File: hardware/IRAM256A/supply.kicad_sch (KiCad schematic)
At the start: 65 parts

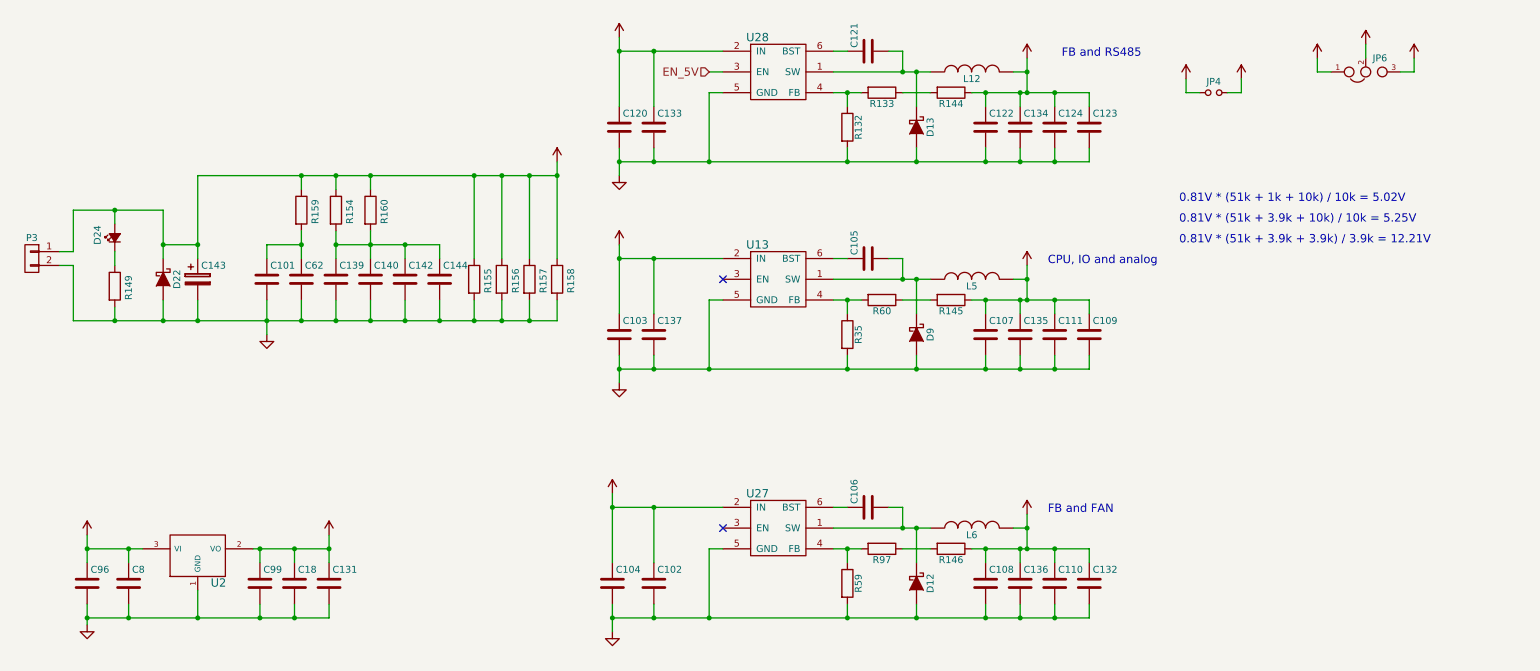
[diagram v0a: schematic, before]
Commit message: Structure change + kicad 3d models updated
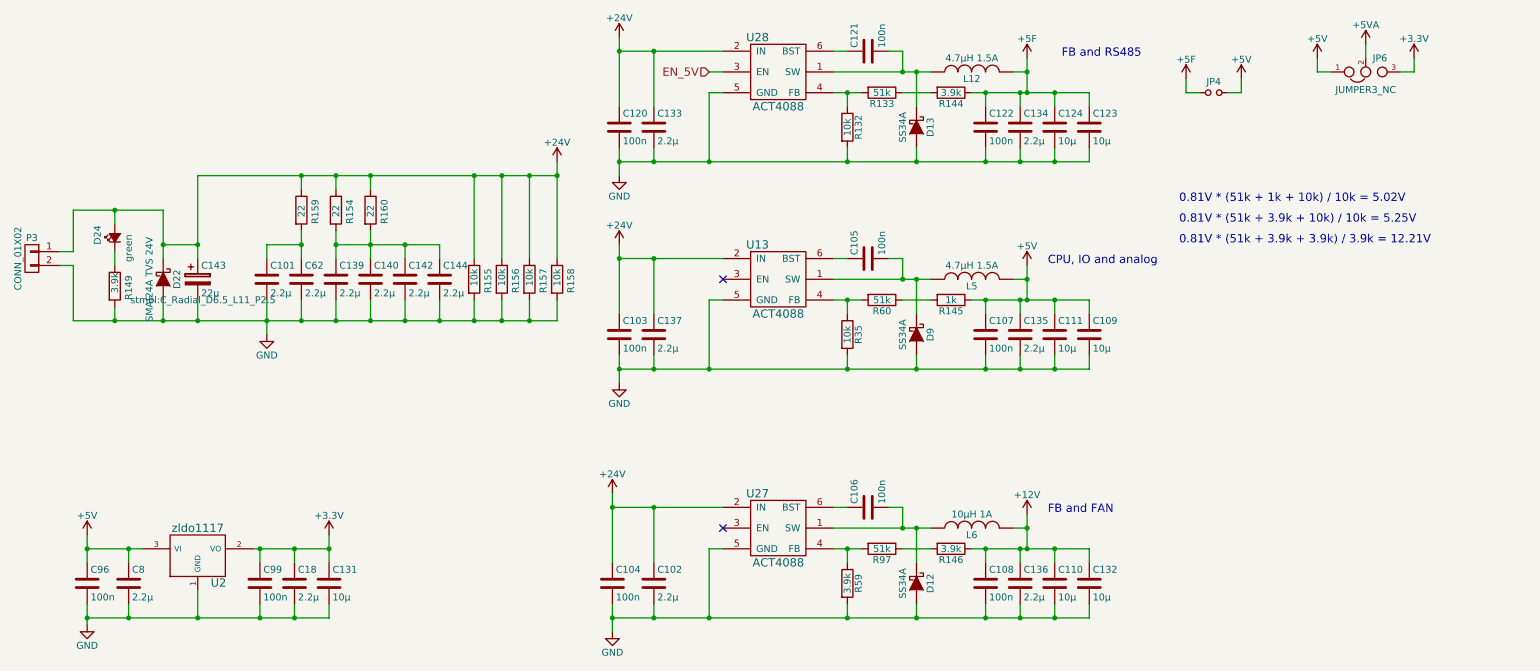
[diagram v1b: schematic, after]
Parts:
- C101, C102, C133, C134, C135, C136, C137, C139, C140, C142, C144, C18, C62, C8: value (none) -> 2.2µ; footprint (none) -> stmbl:C_0603
- C103, C104, C105, C106, C107, C108, C120, C121, C122, C96, C99: value (none) -> 100n; footprint (none) -> stmbl:C_0603
- C109, C110, C111, C123, C124, C131, C132: value (none) -> 10µ; footprint (none) -> stmbl:C_0805
- C143: value (none) -> 22µ; footprint (none) -> stmbl:C_Radial_D6.5_L11_P2.5
- D12, D13, D9: value (none) -> SS34A; footprint (none) -> stmbl:SMA_Standard
- D22: value (none) -> SMAJ24A TVS 24V; footprint (none) -> stmbl:SMA_Standard
- D24: value (none) -> green; footprint (none) -> stmbl:LED-0805-SIDE
- JP4: value (none) -> Jumper_NO_Small; footprint (none) -> stmbl:SOLDER_JUMPER
- JP6: value (none) -> JUMPER3_NC; footprint (none) -> stmbl:SOLDER_JUMPER_3_NC
- L12, L5: value (none) -> 4.7µH 1.5A; footprint (none) -> stmbl:SMD_INDUCTOR_32x25
- L6: value (none) -> 10µH 1A; footprint (none) -> stmbl:SMD_INDUCTOR_32x25
- P3: value (none) -> CONN_01X02; footprint (none) -> stmbl:RM3.5_1x2
- R132, R155, R156, R157, R158, R35: value (none) -> 10k; footprint (none) -> stmbl:R_0603
- R133, R60, R97: value (none) -> 51k; footprint (none) -> stmbl:R_0603
- R144, R146, R149, R59: value (none) -> 3.9k; footprint (none) -> stmbl:R_0603
- R145: value (none) -> 1k; footprint (none) -> stmbl:R_0603
- R154, R159, R160: value (none) -> 22; footprint (none) -> stmbl:R_0603
- U13, U27, U28: value (none) -> ACT4088; footprint (none) -> stmbl:SOT-23-6
- U2: value (none) -> zldo1117; footprint (none) -> stmbl:SOT-223

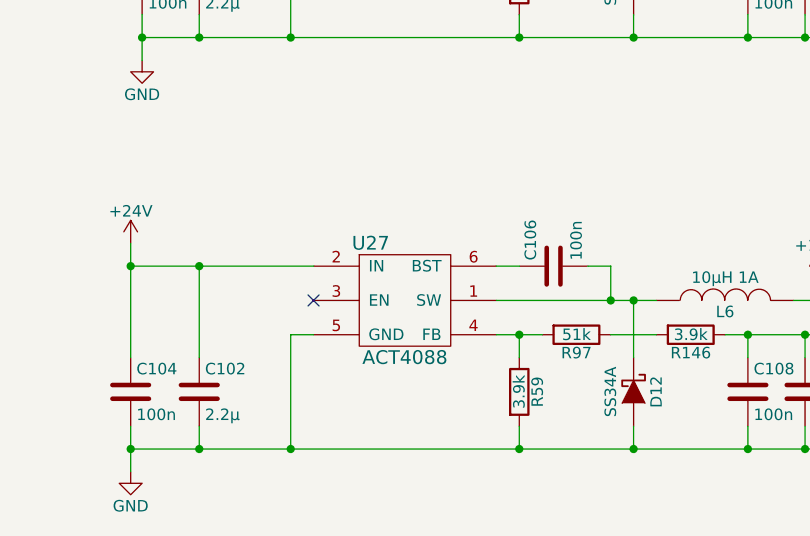
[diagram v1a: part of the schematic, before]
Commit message: Update some package (3D models) + replaced ACT4088 with AOZ1280
AOZ1280 is quite similar to the act4088 with the benefit of being still available for a reasonable price. with the drawback of pinout being different. The schematic had to be moved around and is no longer the same for the three voltage levels.
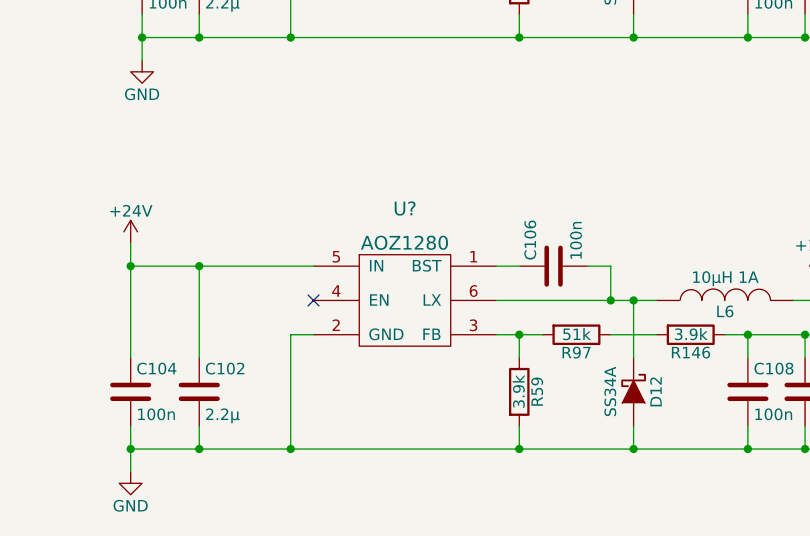
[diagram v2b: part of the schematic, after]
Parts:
- removed U27: ACT4088, stmbl:SOT-23-6, symbol stmbl_4.0-rescue:ACT4088-stmbl
- added U?: AOZ1280, Package_TO_SOT_SMD:SOT-23-6, symbol stmbl:AOZ1280
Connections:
- net +24V: now also U?.5 (IN)
- net GND: now also U?.2 (GND)
- net at R59.1, R97.2: now also U?.3 (FB)
- net at C106.2, D12.1 (K), L6.1: now also U?.6 (LX)
- net at C106.1: now also U?.1 (BST)

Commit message: intermediate update
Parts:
- U13, U28: value ACT4088 -> AOZ1280; footprint stmbl:SOT-23-6 -> Package_TO_SOT_SMD:SOT-23-6; symbol stmbl_4.0-rescue:ACT4088-stmbl -> stmbl:AOZ1280
- gave numbers to parts that had none: 1
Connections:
- net +24V: now also U13.5 (IN), U28.5 (IN); no longer U13.2 (IN), U28.2 (IN)
- net EN_5V: now also U28.4 (EN); no longer U28.3 (EN)
- net GND: now also U13.2 (GND), U28.2 (GND); no longer U13.5 (GND), U28.5 (GND)
- net at R35.1, R60.2: now also U13.3 (FB); no longer U13.4 (FB)
- net at C105.2, D9.1 (K), L5.1: now also U13.6 (LX); no longer U13.1 (SW)
- net at C105.1: now also U13.1 (BST); no longer U13.6 (BST)
- net at R132.1, R133.2: now also U28.3 (FB); no longer U28.4 (FB)
- net at C121.2, D13.1 (K), L12.1: now also U28.6 (LX); no longer U28.1 (SW)
- net at C121.1: now also U28.1 (BST); no longer U28.6 (BST)
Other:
- note added: "0.8V * (51k + 1k + 10k) / 10k = 4.96V"
- note added: "0.8V * (51k + 3.9k + 10k) / 10k = 5.192V"
- note added: "0.8V * (51k + 3.9k + 3.9k) / 3.9k = 12.06V"
- note added: "AOZ1280 Calculations"
- note removed: "0.81V * (51k + 1k + 10k) / 10k = 5.02V"
- note removed: "0.81V * (51k + 3.9k + 10k) / 10k = 5.25V"
- note removed: "0.81V * (51k + 3.9k + 3.9k) / 3.9k = 12.21V"
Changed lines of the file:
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@@
     (stroke (width 0) (type default) (color 0 0 0 0))
   )
-  (text "0.81V * (51k + 3.9k + 3.9k) / 3.9k = 12.21V" (at 231.14 73.66 0)
+  (text "0.8V * (51k + 3.9k + 3.9k) / 3.9k = 12.06V" (at 226.06 97.79 0)
     (effects (font (size 1.524 1.524)) (justify left bottom))
   )
-  (text "0.81V * (51k + 3.9k + 10k) / 10k = 5.25V" (at 231.14 69.85 0)
+  (text "0.8V * (51k + 3.9k + 10k) / 10k = 5.192V" (at 226.06 93.98 0)
     (effects (font (size 1.524 1.524)) (justify left bottom))
   )
-  (text "0.81V * (51k + 1k + 10k) / 10k = 5.02V" (at 231.14 66.04 0)
+  (text "0.8V * (51k + 1k + 10k) / 10k = 4.96V" (at 226.06 90.17 0)
     (effects (font (size 1.524 1.524)) (justify left bottom))
   )
   (text "FB and FAN" (at 207.01 123.19 0)
+    (effects (font (size 1.524 1.524)) (justify left bottom))
+  )
+  (text "AOZ1280 Calculations" (at 237.49 85.09 0)
     (effects (font (size 1.524 1.524)) (justify left bottom))
   )
@@
     (pin "2")
   )
-  (symbol (lib_id "stmbl_4.0-rescue:ACT4088-stmbl") (at 157.48 80.01 0) (unit 1)
+  (symbol (lib_id "stmbl:AOZ1280") (at 157.48 80.01 0) (unit 1)
     (in_bom yes) (on_board yes)
     (property "Reference" "U13" (id 0) (at 153.67 73.66 0)
       (effects (font (size 1.524 1.524)))
     )
-    (property "Value" "ACT4088" (id 1) (at 157.48 86.36 0)
-      (effects (font (size 1.524 1.524)))
-    )
-    (property "Footprint" "stmbl:SOT-23-6" (id 2) (at 157.48 80.01 0)
-      (effects (font (size 1.524 1.524)) hide)
-    )
-    (property "Datasheet" "" (id 3) (at 157.48 80.01 0)
-      (effects (font (size 1.524 1.524)))
+    (property "Value" "AOZ1280" (id 1) (at 157.48 86.36 0)
+      (effects (font (size 1.524 1.524)))
+    )
+    (property "Footprint" "Package_TO_SOT_SMD:SOT-23-6" (id 2) (at 157.48 80.01 0)
+      (effects (font (size 1.524 1.524)) hide)
+    )
+    (property "Datasheet" "https://www.tme.eu/Document/921be39cd2271a5b3bfe03eff0ec2438/AOZ1280CI-DTE.pdf" (id 3) (at 157.48 80.01 0)
+      (effects (font (size 1.524 1.524)) hide)
     )
     (property "InternalName" "" (id 4) (at 157.48 80.01 0)
@@
     (pin "2")
   )
-  (symbol (lib_id "stmbl_4.0-rescue:ACT4088-stmbl") (at 157.48 41.91 0) (unit 1)
+  (symbol (lib_id "stmbl:AOZ1280") (at 157.48 41.91 0) (unit 1)
     (in_bom yes) (on_board yes)
     (property "Reference" "U28" (id 0) (at 153.67 35.56 0)
       (effects (font (size 1.524 1.524)))
     )
-    (property "Value" "ACT4088" (id 1) (at 157.48 48.26 0)
-      (effects (font (size 1.524 1.524)))
-    )
-    (property "Footprint" "stmbl:SOT-23-6" (id 2) (at 157.48 41.91 0)
-      (effects (font (size 1.524 1.524)) hide)
-    )
-    (property "Datasheet" "" (id 3) (at 157.48 41.91 0)
-      (effects (font (size 1.524 1.524)))
+    (property "Value" "AOZ1280" (id 1) (at 157.48 48.26 0)
+      (effects (font (size 1.524 1.524)))
+    )
+    (property "Footprint" "Package_TO_SOT_SMD:SOT-23-6" (id 2) (at 157.48 41.91 0)
+      (effects (font (size 1.524 1.524)) hide)
+    )
+    (property "Datasheet" "https://www.tme.eu/Document/921be39cd2271a5b3bfe03eff0ec2438/AOZ1280CI-DTE.pdf" (id 3) (at 157.48 41.91 0)
+      (effects (font (size 1.524 1.524)) hide)
     )
     (property "InternalName" "" (id 4) (at 157.48 41.91 0)
@@
   (symbol (lib_id "stmbl:AOZ1280") (at 157.48 125.73 0) (unit 1)
     (in_bom yes) (on_board yes) (fields_autoplaced)
-    (property "Reference" "U?" (id 0) (at 157.48 115.57 0)
-      (effects (font (size 1.524 1.524)))
-    )
+    (property "Reference" "U27" (id 0) (at 157.48 115.57 0)
+      (effects (font (size 1.524 1.524)))
+    )
